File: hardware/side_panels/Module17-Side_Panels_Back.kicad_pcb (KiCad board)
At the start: 2 copper layers, 103 x 30.5 mm, 6 parts

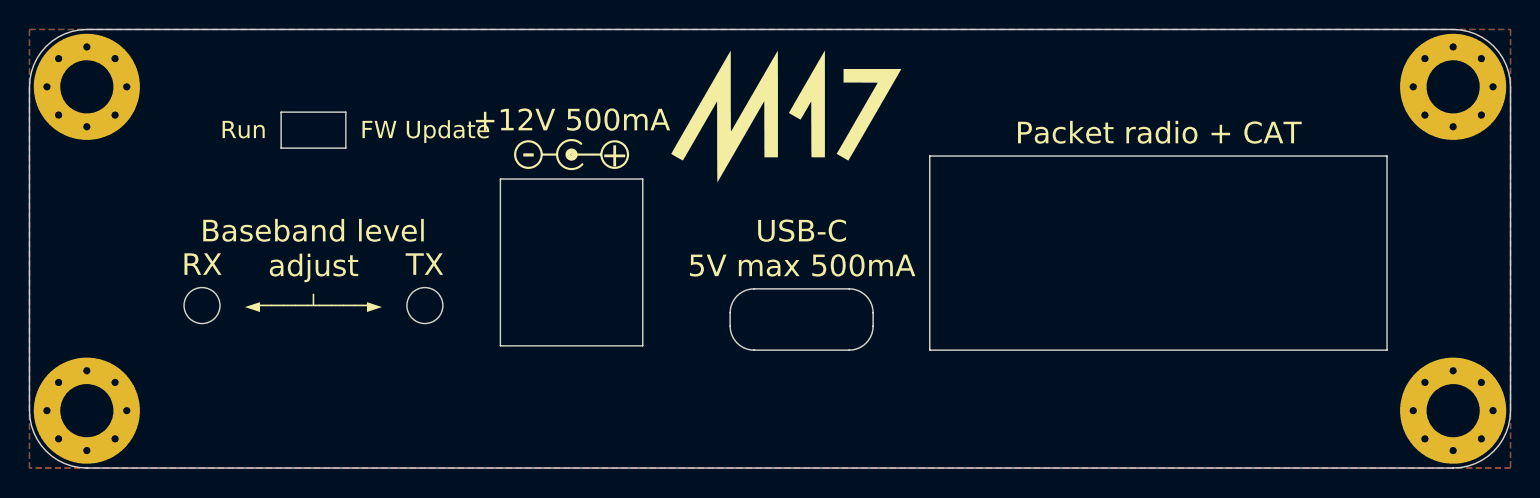
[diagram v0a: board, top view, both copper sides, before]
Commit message: Updated Side Panels to Rev 0.99b
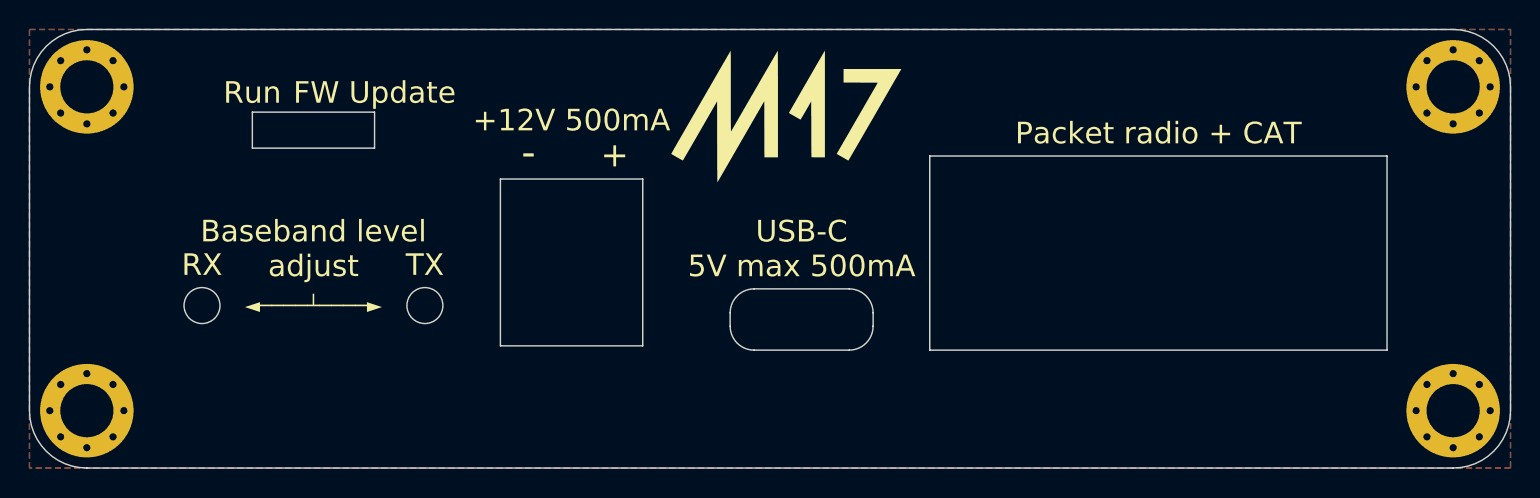
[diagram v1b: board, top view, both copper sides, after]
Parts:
- removed REF**: Symbol_Barrel_Polarity, Symbol:Symbol_Barrel_Polarity
- H1, H2, H3, H4: footprint MountingHole:MountingHole_3.7mm_Pad_Via -> M17_mounting_hole:MountingHole_3.7mm_Pad_Via_Small_Pad
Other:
- outline, holes or cut-outs redrawn
- board text added: "Module17 HMI Back panel Rev 0.99b by Morgan ON4MOD"
- board text removed: "Module17 HMI Back panel Rev 0.99 by Morgan ON4MOD"

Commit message: Updated side panels PCBs to revision 1.0
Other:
- board text added: "Module17 HMI Back panel Rev 1.0 by Morgan ON4MOD"
- board text removed: "Module17 HMI Back panel Rev 0.99b by Morgan ON4MOD"

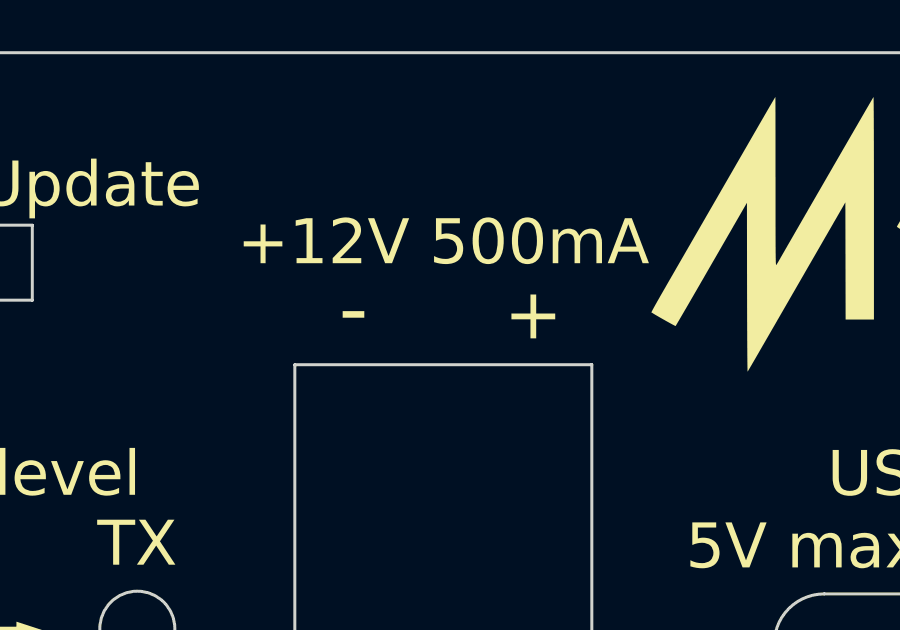
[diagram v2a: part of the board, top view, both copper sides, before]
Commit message: Fixed missing symbol
Barrel polarity symbol was missing. No electrical or functional changes.
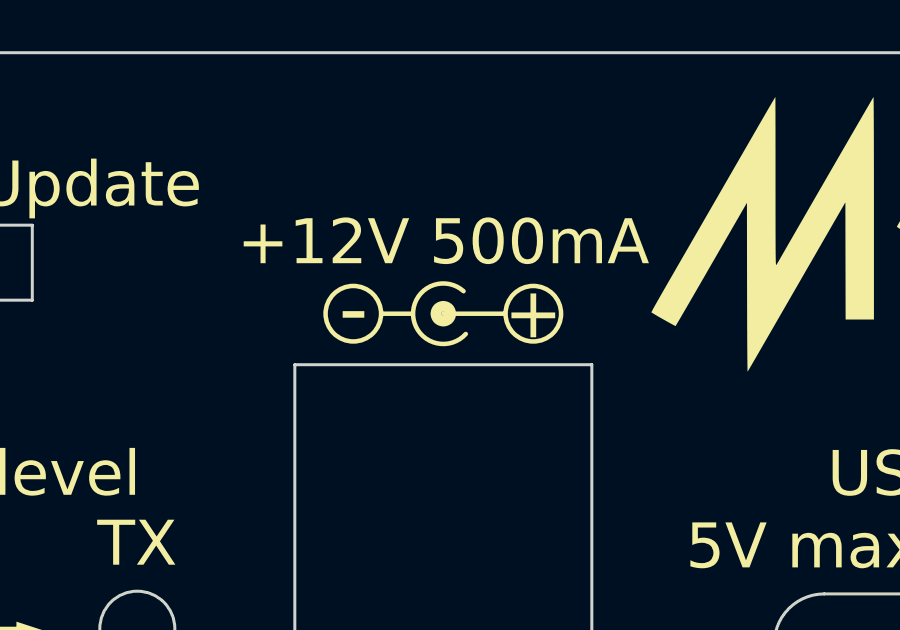
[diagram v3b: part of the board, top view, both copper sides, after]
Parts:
- added REF**: Symbol_Barrel_Polarity, Symbol:Symbol_Barrel_Polarity, F.Cu at (100.6, 98.6)
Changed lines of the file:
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@@
+		)
+	)
+	(footprint "Symbol:Symbol_Barrel_Polarity"
+		(layer "F.Cu")
+		(at 100.575 98.57)
+		(descr "Barrel connector polarity indicator")
+		(tags "barrel polarity")
+		(property "Reference" "REF**"
+			(at 0 -2 0)
+			(layer "F.SilkS")
+			(hide yes)
+			(effects
+				(font
+					(size 1 1)
+					(thickness 0.15)
+				)
+			)
+		)
+		(property "Value" "Symbol_Barrel_Polarity"
+			(at 0 2 0)
+			(layer "F.Fab")
+			(effects
+				(font
+					(size 1 1)
+					(thickness 0.15)
+				)
+			)
+		)
+		(property "Footprint" "Symbol:Symbol_Barrel_Polarity"
+			(at 0 0 0)
+			(unlocked yes)
+			(layer "F.Fab")
+			(hide yes)
+			(effects
+				(font
+					(size 1.27 1.27)
+					(thickness 0.15)
+				)
+			)
+		)
+		(property "Datasheet" ""
+			(at 0 0 0)
+			(unlocked yes)
+			(layer "F.Fab")
+			(hide yes)
+			(effects
+				(font
+					(size 1.27 1.27)
+					(thickness 0.15)
+				)
+			)
+		)
+		(property "Description" ""
+			(at 0 0 0)
+			(unlocked yes)
+			(layer "F.Fab")
+			(hide yes)
+			(effects
+				(font
+					(size 1.27 1.27)
+					(thickness 0.15)
+				)
+			)
+		)
+		(attr exclude_from_pos_files exclude_from_bom allow_missing_courtyard)
+		(fp_line
+			(start -2 0.075)
+			(end -1.1 0.075)
+			(stroke
+				(width 0.15)
+				(type solid)
+			)
+			(layer "F.SilkS")
+		)
+		(fp_line
+			(start 0 0.075)
+			(end 2 0.075)
+			(stroke
+				(width 0.15)
+				(type solid)
+			)
+			(layer "F.SilkS")
+		)
+		(fp_arc
+			(start 0.75 0.75)
+			(mid -1.007627 0.128033)
+			(end 0.675 -0.675)
+			(stroke
+				(width 0.15)
+				(type solid)
+			)
+			(layer "F.SilkS")
+		)
+		(fp_circle
+			(center -3 0.075)
+			(end -3 1)
+			(stroke
+				(width 0.15)
+				(type solid)
+			)
+			(fill none)
+			(layer "F.SilkS")
+		)
+		(fp_circle
+			(center 0 0.075)
+			(end 0 0.25)
+			(stroke
+				(width 0.5)
+				(type solid)
+			)
+			(fill none)
+			(layer "F.SilkS")
+		)
+		(fp_circle
+			(center 3 0.075)
+			(end 3 1)
+			(stroke
+				(width 0.15)
+				(type solid)
+			)
+			(fill none)
+			(layer "F.SilkS")
 		)
 	)
@@
 	)
 	(gr_text "+"
-		(at 103.575 98.68 0)
+		(at 103.575 98.645 0)
 		(layer "F.SilkS")
 		(effects
@@
 			(polygon
 				(pts
-					(xy 103.503999 99.119764) (xy 103.503999 98.72116) (xy 103.099582 98.72116) (xy 103.099582 98.588292)
-					(xy 103.503999 98.588292) (xy 103.503999 98.163114) (xy 103.646832 98.163114) (xy 103.646832 98.588292)
-					(xy 104.051249 98.588292) (xy 104.051249 98.72116) (xy 103.646832 98.72116) (xy 103.646832 99.119764)
-				)
-			)
+					(xy 103.503999 99.084764) (xy 103.503999 98.68616) (xy 103.099582 98.68616) (xy 103.099582 98.553292)
+					(xy 103.503999 98.553292) (xy 103.503999 98.128114) (xy 103.646832 98.128114) (xy 103.646832 98.553292)
+					(xy 104.051249 98.553292) (xy 104.051249 98.68616) (xy 103.646832 98.68616) (xy 103.646832 99.084764)
+				)
+			)
